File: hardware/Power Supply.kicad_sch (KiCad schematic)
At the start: 12 parts, among them J5 Battery_In, J6 5V Out, U2 LM2596S-ADJ

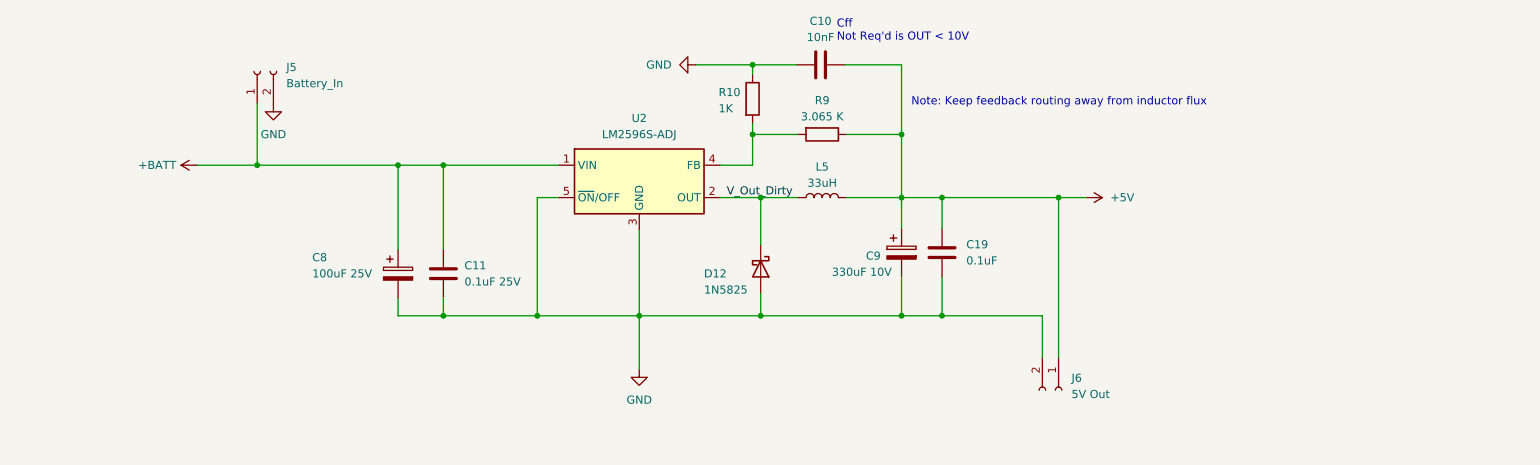
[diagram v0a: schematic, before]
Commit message: Hardware V0.2 - Schematics update
Combines Cell holder, BMS, and voltage regulator into single board
complete w. extensive electrical and thermal protections including:

* MM3220 BMS w Overvoltage, Overcurrent, undervoltage charging/discharge protect
* Fuses on cells, 12v in, 5v and 8.4v out.
* Reverse polarity protection on 12v and cells.

Adds debug UART header
Single IO header on every board
Minor component size corrections
Add current limiting resistor to RPI power NMOS gate.
Add optional support for MLCC/tantalum caps for Voltage Regulator instead of electrolytic
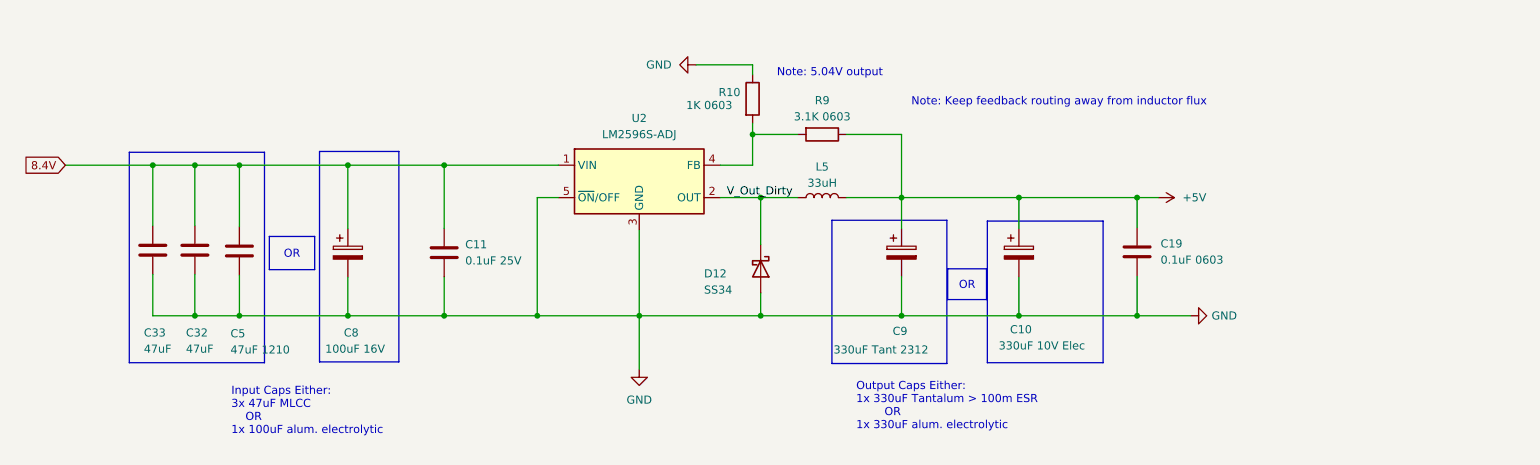
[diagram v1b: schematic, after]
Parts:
- removed C10: 10nF, Capacitor_SMD:C_0504_1310Metric_Pad0.83x1.28mm_HandSolder, symbol Device:C
- removed J5: Battery_In, Connector_PinHeader_2.54mm:PinHeader_1x02_P2.54mm_Vertical, symbol Connector:Conn_01x02_Socket
- removed J6: 5V Out, Connector_PinHeader_2.54mm:PinHeader_1x02_P2.54mm_Vertical, symbol Connector:Conn_01x02_Socket
- added C10: 330uF 10V Elec, Capacitor_SMD:C_0603_1608Metric_Pad1.08x0.95mm_HandSolder, symbol Device:C_Polarized
- added C32, C33: 47uF, Resistor_SMD:R_1210_3225Metric_Pad1.30x2.65mm_HandSolder, symbol Device:C
- added C5: 47uF 1210, Resistor_SMD:R_1210_3225Metric_Pad1.30x2.65mm_HandSolder, symbol Device:C
- C11: footprint Capacitor_SMD:C_0504_1310Metric_Pad0.83x1.28mm_HandSolder -> Capacitor_SMD:C_0603_1608Metric_Pad1.08x0.95mm_HandSolder
- C19: value 0.1uF -> 0.1uF 0603; footprint Capacitor_SMD:C_0504_1310Metric_Pad0.83x1.28mm_HandSolder -> Capacitor_SMD:C_0603_1608Metric_Pad1.08x0.95mm_HandSolder
- C8: value 100uF 25V -> 100uF 16V; footprint Capacitor_SMD:CP_Elec_6.3x5.9 -> Capacitor_SMD:C_0603_1608Metric_Pad1.08x0.95mm_HandSolder
- C9: value 330uF 10V -> 330uF Tant 2312; footprint Capacitor_SMD:CP_Elec_6.3x5.9 -> Capacitor_SMD:C_0603_1608Metric_Pad1.08x0.95mm_HandSolder
- D12: value 1N5825 -> SS34; footprint Diode_SMD:D_SMA-SMB_Universal_Handsoldering -> Diode_SMD:D_SMA_Handsoldering
- L5: footprint Inductor_SMD:L_Bourns_SRP7028A_7.3x6.6mm -> Inductor - 125CDMCCDS 33uH:IND_125CDMCCDS-330MC
- R10: value 1K -> 1K 0603
- R9: value 3.065 K -> 3.1K 0603
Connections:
- net +5V: now also C10.1
- net GND: now also C10.2, C32.2, C33.2, C5.2
- net +BATT renamed 8.4V
- net 8.4V: now also C32.1, C33.1, C5.1
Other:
- note added: "Input Caps Either: 3x 47uF MLCC OR 1x 100uF alum. electrolytic"
- note added: "Note: 5.04V output"
- note added: "Output Caps Either: 1x 330uF Tantalum > 100m ESR OR 1x 330uF alum. electrolytic"
- note removed: "Cff Not Req'd is OUT < 10V"
- moved on the sheet: C11, C19, C8

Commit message: Hardware revision 0.2 routing
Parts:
- added F2: 2.2A Polyfuse 1210, Fuse:Fuse_1210_3225Metric_Pad1.42x2.65mm_HandSolder, symbol Device:Polyfuse
- C10: footprint Capacitor_SMD:C_0603_1608Metric_Pad1.08x0.95mm_HandSolder -> Capacitor_SMD:C_Elec_6.3x7.7
- C8: footprint Capacitor_SMD:C_0603_1608Metric_Pad1.08x0.95mm_HandSolder -> Capacitor_SMD:CP_Elec_6.3x7.7
- C9: footprint Capacitor_SMD:C_0603_1608Metric_Pad1.08x0.95mm_HandSolder -> C _Tantalum - TAJC337K006RNJ:CAPPM6032X280N
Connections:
- net 8.4V: now also F2.1; no longer C11.1, C32.1, C33.1, C5.1, C8.1, U2.1 (VIN)
- new net Vin_clean: C11.1, C32.1, C33.1, C5.1, C8.1, F2.2, U2.1 (VIN)
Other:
- company: (none) -> KBader94
- title: (none) -> OpenActionCam
- moved on the sheet: C10, C11, C19, C32, C33, C5, C8, C9, D12, L5, R10, R9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
